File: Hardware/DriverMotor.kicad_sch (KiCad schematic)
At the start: 13 parts, among them J2 Screw_Terminal_01x02, U3 XL1509-5.0

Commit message: Update Sche
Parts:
- added C10: 100nF, IVS_FOOTPRINTS:C_0603, symbol IVS_SYMBOLS:C
- added C11: 10uF, IVS_FOOTPRINTS:C_0603, symbol IVS_SYMBOLS:C
- added C23: 4.7uF/16V, Capacitor_SMD:CP_Elec_4x5.4, symbol Device:C
- added C24: 10uF/16V, Capacitor_SMD:CP_Elec_4x5.4, symbol Device:C
- added R24: 120R, IVS_FOOTPRINTS:R_0603, symbol IVS_SYMBOLS:R
- added U11: B0505S, IVS_FOOTPRINTS:B0505S, symbol IVS_SYMBOLS:B0505S
- added U9: LD1117, IVS_FOOTPRINTS:SOT233, symbol IVS_SYMBOLS:LD1117
- C14: footprint IVS_FOOTPRINTS:CP-Radial-DIP-D12.0mm-P5.00mm -> Capacitor_THT:CP_Radial_D10.0mm_P5.00mm
- F1: value 30V/1.1A -> 30V/5A; footprint Fuse:Fuse_Bourns_MF-RG300 -> Fuse:Fuse_Bourns_MF-RHT1000
- L2: footprint Inductor_SMD:L_6.3x6.3_H3 -> Inductor_SMD:L_1812_4532Metric
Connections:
- net +5V_CS: now also C24.1, U11.4 (Vout); no longer C16.1, C17.2, L2.1, R10.1, R9.2
- net GNDD: now also C24.2, U11.3 (GNDout); no longer J2.2 (Pin_2)
- new net +3V3: C11.1, R24.1, U9.2 (VO)
- new net +5V: C10.1, C16.1, C17.2, C23.1, L2.1, R10.1, R9.2, U11.2 (Vin), U9.3 (VI)
- new net GND: C10.2, C11.2, C23.2, J2.2 (Pin_2), R24.2, U11.1 (GNDin), U9.1 (GND)

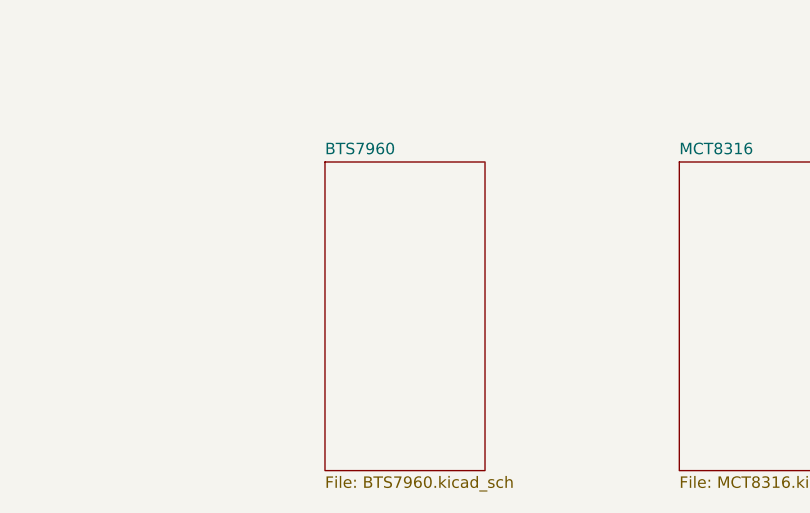
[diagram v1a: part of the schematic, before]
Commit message: Hie BTS, fix GND opto MCT
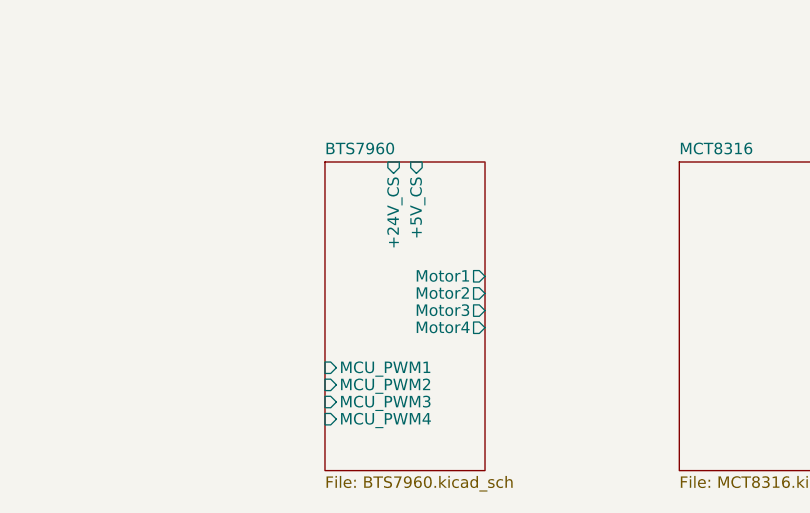
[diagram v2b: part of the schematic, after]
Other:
- sheet BTS7960 ports: added +24V_CS, +5V_CS, MCU_PWM1, MCU_PWM2, MCU_PWM3, MCU_PWM4, Motor1, Motor2, Motor3, Motor4; removed none
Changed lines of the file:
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@@
       (effects (font (size 1.27 1.27)) (justify left top))
+    )
+    (pin "+24V_CS" input (at 125.73 106.68 90)
+      (effects (font (size 1.27 1.27)) (justify right))
+    )
+    (pin "+5V_CS" input (at 128.27 106.68 90)
+      (effects (font (size 1.27 1.27)) (justify right))
+    )
+    (pin "Motor1" output (at 135.89 119.38 0)
+      (effects (font (size 1.27 1.27)) (justify right))
+    )
+    (pin "Motor2" output (at 135.89 121.285 0)
+      (effects (font (size 1.27 1.27)) (justify right))
+    )
+    (pin "MCU_PWM1" input (at 118.11 129.54 180)
+      (effects (font (size 1.27 1.27)) (justify left))
+    )
+    (pin "MCU_PWM2" input (at 118.11 131.445 180)
+      (effects (font (size 1.27 1.27)) (justify left))
+    )
+    (pin "Motor4" output (at 135.89 125.095 0)
+      (effects (font (size 1.27 1.27)) (justify right))
+    )
+    (pin "Motor3" output (at 135.89 123.19 0)
+      (effects (font (size 1.27 1.27)) (justify right))
+    )
+    (pin "MCU_PWM3" input (at 118.11 133.35 180)
+      (effects (font (size 1.27 1.27)) (justify left))
+    )
+    (pin "MCU_PWM4" input (at 118.11 135.255 180)
+      (effects (font (size 1.27 1.27)) (justify left))
     )
     (instances

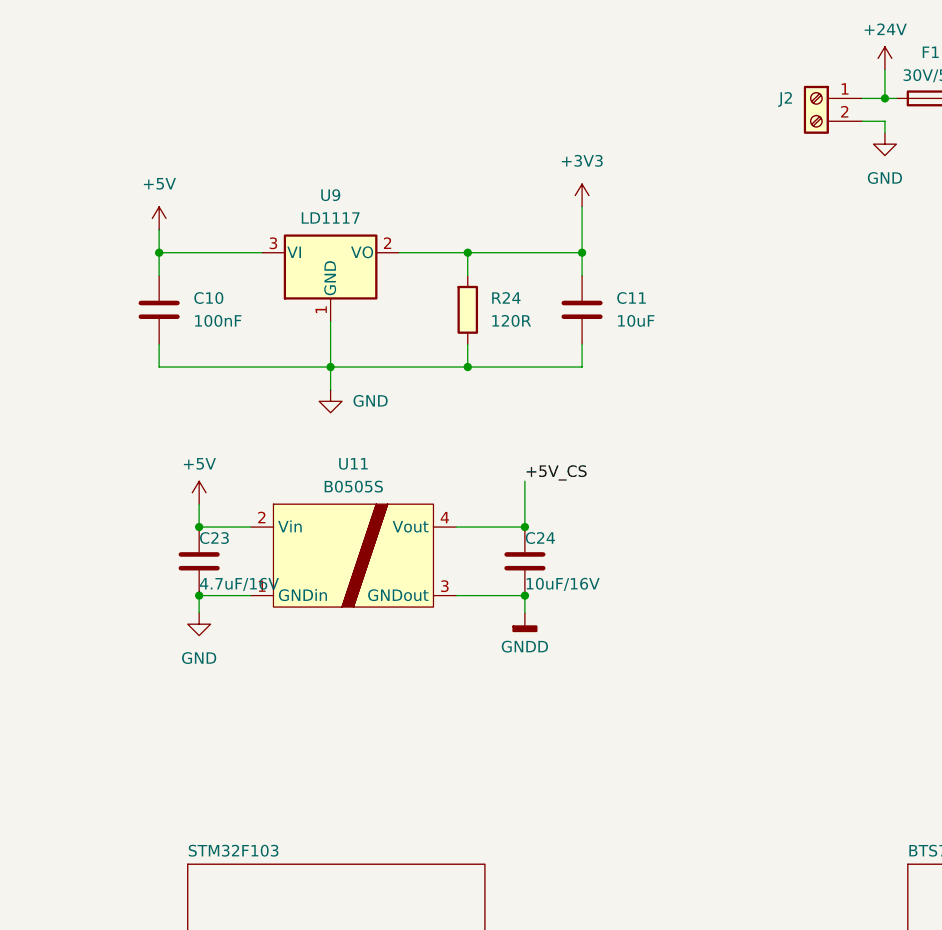
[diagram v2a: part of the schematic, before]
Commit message: Add cap 10uF and 100nF of LD1117
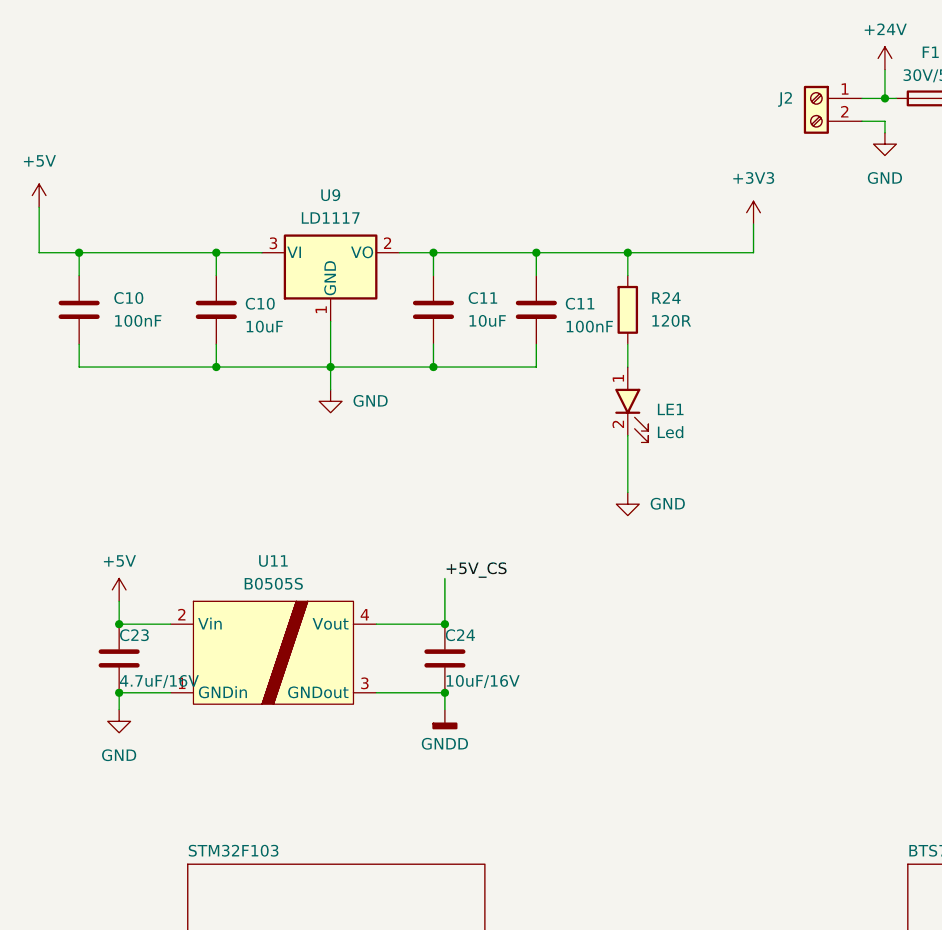
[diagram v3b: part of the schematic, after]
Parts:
- added C10: 10uF, IVS_FOOTPRINTS:C_0603, symbol IVS_SYMBOLS:C
- added C11: 100nF, IVS_FOOTPRINTS:C_0603, symbol IVS_SYMBOLS:C
- added LE1: Led, symbol IVS_SYMBOLS:Led
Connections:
- net +3V3: now also C11.1
- net +5V: now also C10.1
- net GND: now also C10.2, C11.2, LE1.2; no longer R24.2
- new net: LE1.1, R24.2
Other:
- moved on the sheet: C10, C11, C23, C24, U11

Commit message: Up schematic
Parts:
- removed C17: 3.3nF, IVS_FOOTPRINTS:C_0603, symbol Device:C
- removed R8: 1K, IVS_FOOTPRINTS:R_0603, symbol Device:R
- removed R9: 3K1, IVS_FOOTPRINTS:R_0603, symbol Device:R
- C14: value 470uF/50V -> 470uF/35V; footprint Capacitor_THT:CP_Radial_D10.0mm_P5.00mm -> IVS_FOOTPRINTS:CP-Alu-SMD-10x10.5mm
- C16: value 470uF/35V -> 470uF/16V; footprint IVS_FOOTPRINTS:CP-Radial-DIP-D12.0mm-P5.00mm -> IVS_FOOTPRINTS:CP-Alu-SMD-8x10.5mm
- LE1: footprint (none) -> IVS_FOOTPRINTS:LED_0603
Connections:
- net +24V: now also C14.1, C15.1, U3.1 (VIN)
- net +24V_CS: no longer C14.1, C15.1, U3.1 (VIN)
- net GND: now also C14.2, C15.2, C16.2, D3.2 (A), D4.1 (K), U3.5 (GND), U3.6 (GND), U3.7 (GND), U3.8 (GND)
- net GNDD: no longer C14.2, C15.2, C16.2, D3.2 (A), D4.1 (K), U3.5 (GND), U3.6 (GND), U3.7 (GND), U3.8 (GND)
- net at D3.1 (K), L2.2, U3.2 (OUT): now also U3.3 (FB)
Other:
- added sheet TJA1050 (TJA1050.kicad_sch)
- sheet BTS7960 ports: added none; removed +24V_CS, +5V_CS, MCU_PWM1, MCU_PWM2, MCU_PWM3, MCU_PWM4, Motor1, Motor2, Motor3, Motor4
- moved on the sheet: R10

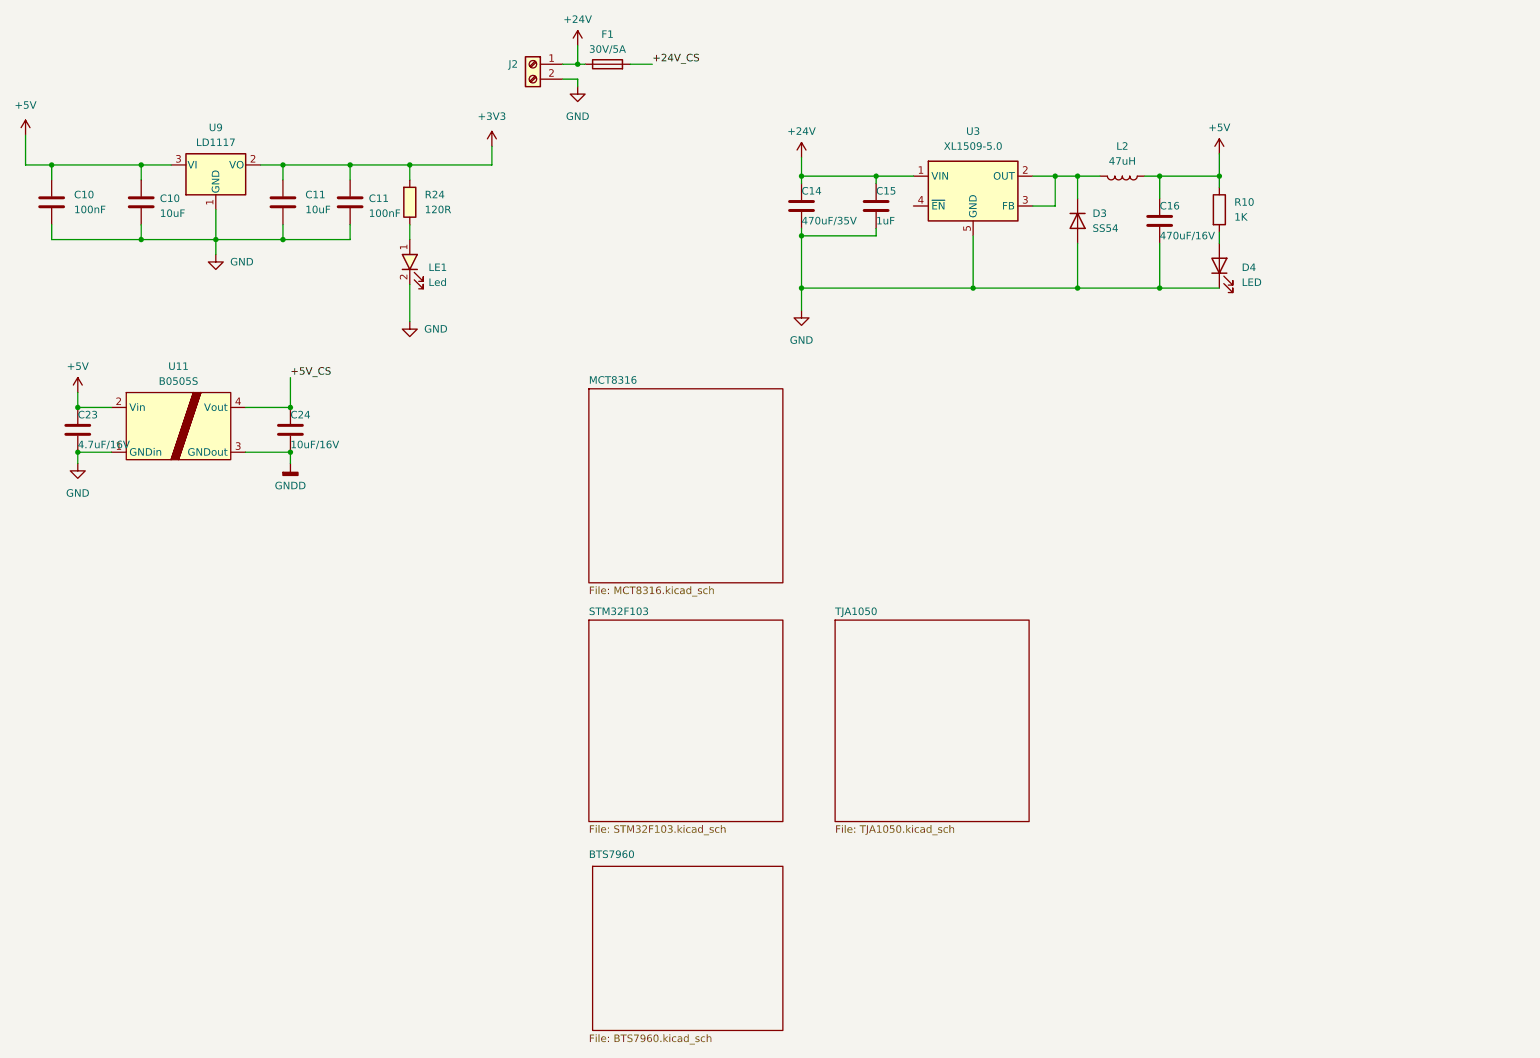
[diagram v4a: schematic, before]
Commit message: Update schematic part2
Vẽ bus dành cho khối BLDC
Đóng khối chức năng cho sheet MCT8316
Tạo sheet nguồn cho các mạch nguồn Buck DCDC, LDO LD1117, BS0505
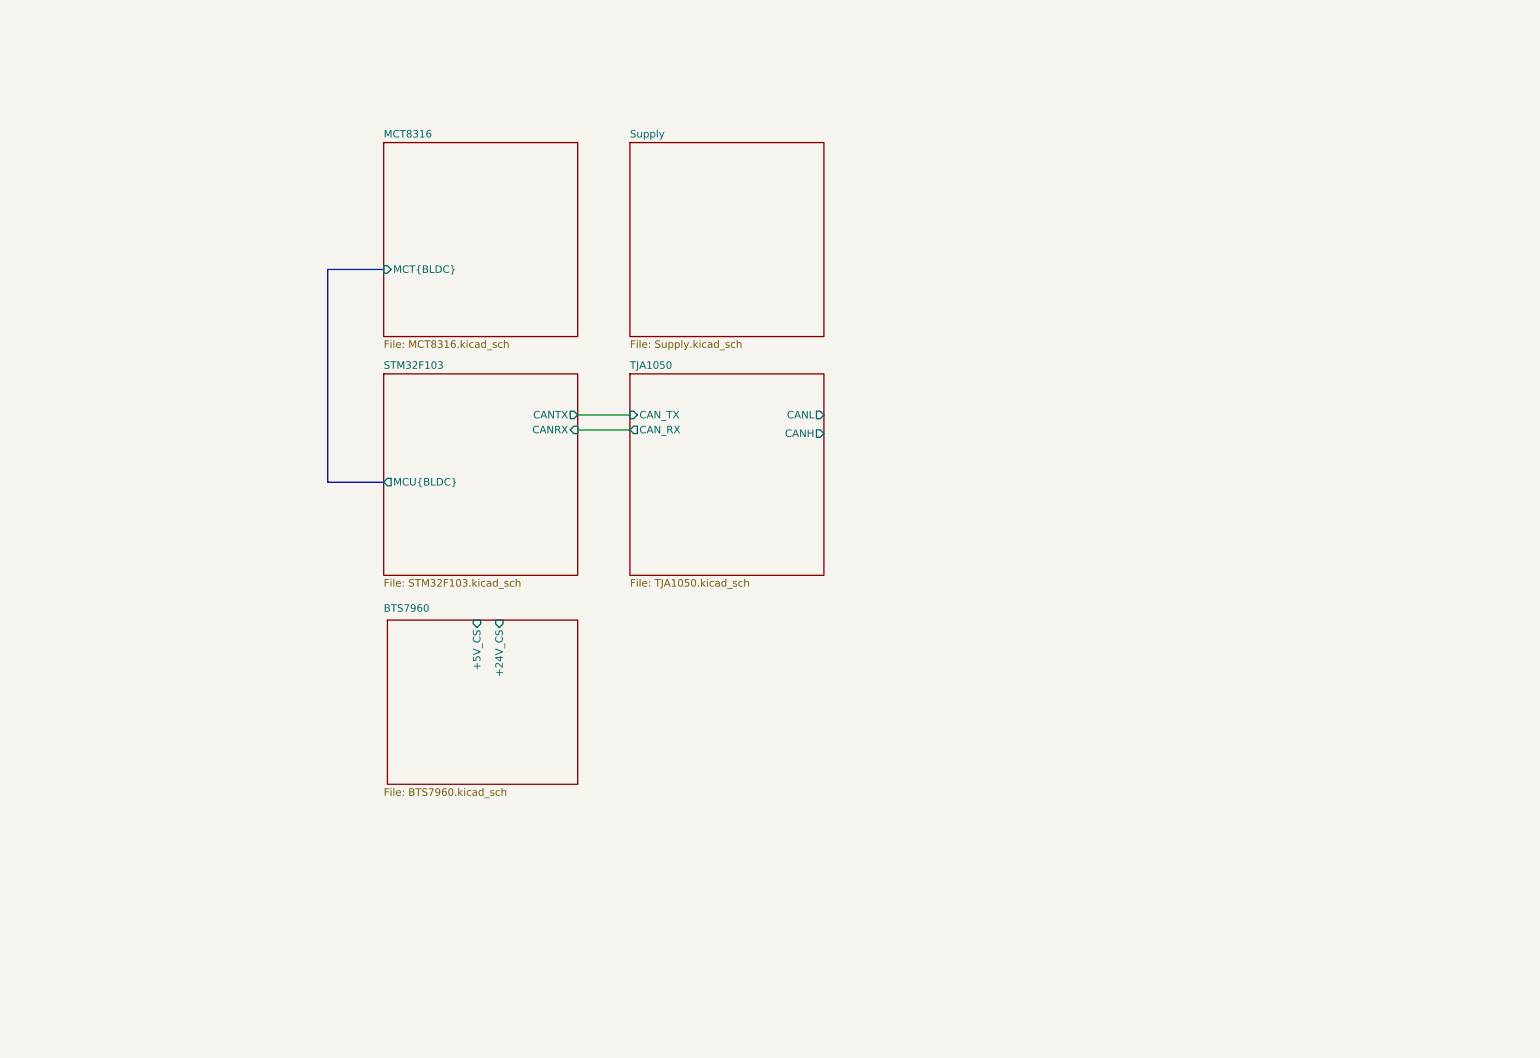
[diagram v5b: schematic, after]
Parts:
- removed C10, C11: 100nF, IVS_FOOTPRINTS:C_0603, symbol IVS_SYMBOLS:C
- removed C10, C11: 10uF, IVS_FOOTPRINTS:C_0603, symbol IVS_SYMBOLS:C
- removed C14: 470uF/35V, IVS_FOOTPRINTS:CP-Alu-SMD-10x10.5mm, symbol Device:C
- removed C15: 1uF, IVS_FOOTPRINTS:C_0603, symbol Device:C
- removed C16: 470uF/16V, IVS_FOOTPRINTS:CP-Alu-SMD-8x10.5mm, symbol Device:C
- removed C23: 4.7uF/16V, Capacitor_SMD:CP_Elec_4x5.4, symbol Device:C
- removed C24: 10uF/16V, Capacitor_SMD:CP_Elec_4x5.4, symbol Device:C
- removed D3: SS54, IVS_FOOTPRINTS:Package-Diode-D_SMA, symbol Device:D
- removed D4: LED, IVS_FOOTPRINTS:LED_0603, symbol Device:LED
- removed F1: 30V/5A, Fuse:Fuse_Bourns_MF-RHT1000, symbol Device:Fuse
- removed J2: Screw_Terminal_01x02, IVS_FOOTPRINTS:Conn-Vert-THT-2P-7.20mm-XT60_F, symbol Connector:Screw_Terminal_01x02
- removed L2: 47uH, Inductor_SMD:L_1812_4532Metric, symbol Device:L
- removed LE1: Led, IVS_FOOTPRINTS:LED_0603, symbol IVS_SYMBOLS:Led
- removed R10: 1K, IVS_FOOTPRINTS:R_0603, symbol Device:R
- removed R24: 120R, IVS_FOOTPRINTS:R_0603, symbol IVS_SYMBOLS:R
- removed U11: B0505S, IVS_FOOTPRINTS:B0505S, symbol IVS_SYMBOLS:B0505S
- removed U3: XL1509-5.0, Package_SO:SOIC-8_3.9x4.9mm_P1.27mm, symbol Regulator_Switching:XL1509-5.0
- removed U9: LD1117, IVS_FOOTPRINTS:SOT233, symbol IVS_SYMBOLS:LD1117
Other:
- added sheet Supply (Supply.kicad_sch)
- sheet BTS7960 ports: added +24V_CS, +5V_CS; removed none
- sheet MCT8316 ports: added MCT{BLDC}; removed none
- sheet STM32F103 ports: added CANRX, CANTX, MCU{BLDC}; removed none
- sheet TJA1050 ports: added CANH, CANL, CAN_RX, CAN_TX; removed none
